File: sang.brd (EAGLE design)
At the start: 92.4 x 80 mm, 27 parts, among them IC1 L293D, IC2 L293D, IC3 NE555, Q1 16MHz

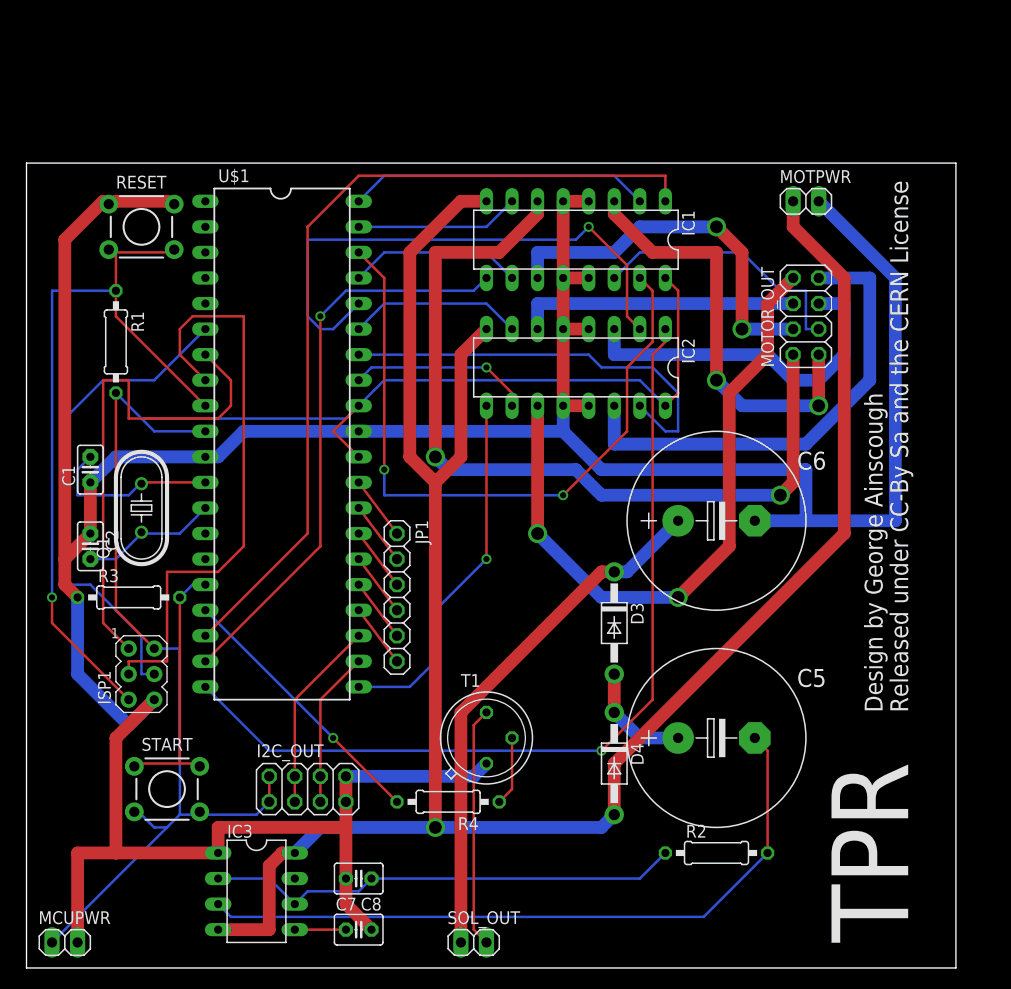
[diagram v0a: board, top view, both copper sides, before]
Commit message: Pins BrokenOut - Pullups Changed
Internal Pull ups to be used, aded I2C pullups
Broke ut unused pin
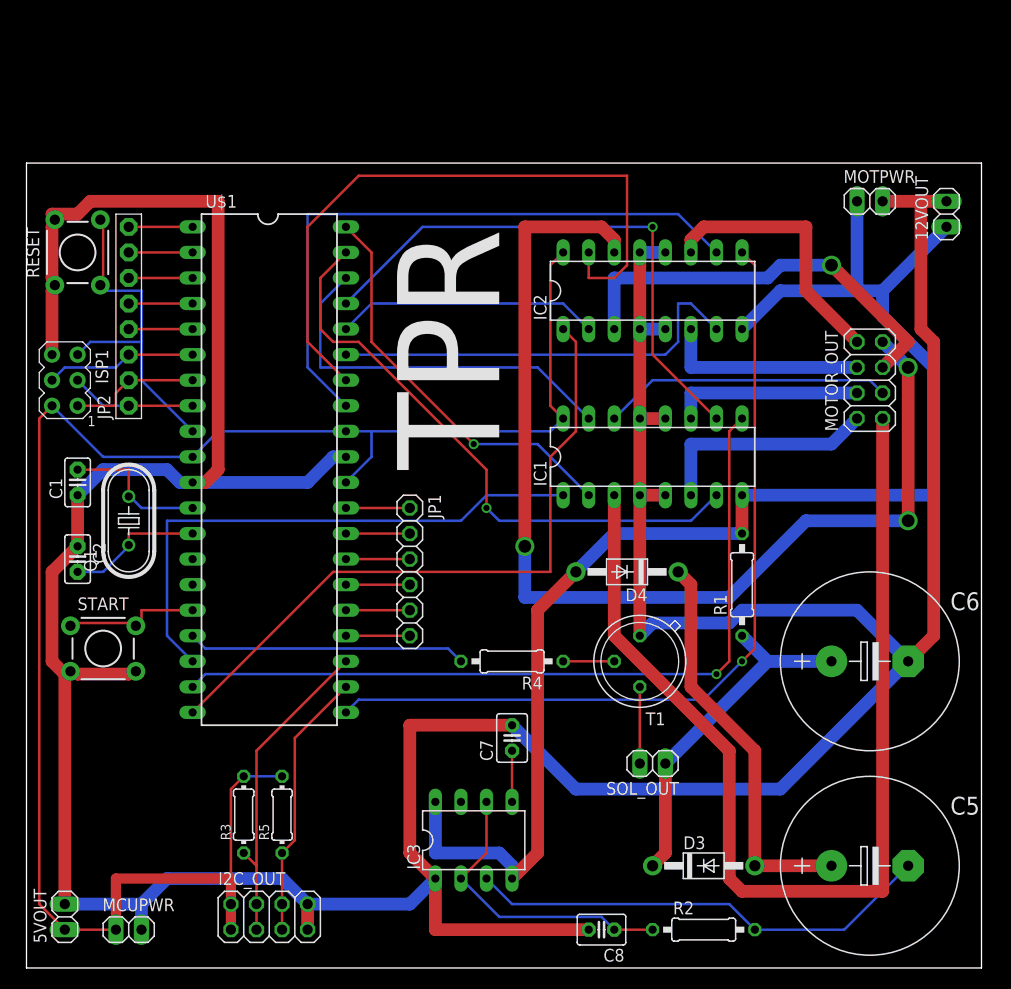
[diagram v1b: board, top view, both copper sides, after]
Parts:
- added 12VOUT, 5VOUT: (no value), pinhead:1X02
- added JP2: (no value), adafruit:1X08-BIG
- added R5: (no value), resistor:0204/7
- R3: value 10K -> (none); device resistor:0207/10 -> resistor:0204/7
- moved R1 66.7 mm to (71.1, 38.1), turned to 90 degrees
- moved ISP1 30.2 mm to (3.81, 58.4), turned to 180 degrees
- moved D3 25.7 mm to (67.3, 10.2), turned to 0 degrees
- moved SOL_OUT 25.1 mm to (62.2, 20.3), turned to 180 degrees
- moved C8 24.7 mm to (57.1, 3.81)
- moved R3 24.4 mm to (21.6, 15.2), turned to 90 degrees
- moved C7 24.4 mm to (48.3, 22.9), turned to 90 degrees
- moved IC1 22.9 mm to (62.2, 50.8), turned to 0 degrees
- moved IC3 22.2 mm to (44.5, 12.7), turned to 0 degrees
- moved C6 20.7 mm to (83.8, 30.5)
- moved C5 19.8 mm to (83.8, 10.2)
- moved D4 19.1 mm to (59.7, 39.4), turned to 180 degrees
- moved T1 17.0 mm to (61.0, 30.5), turned to 180 degrees
- moved R4 15.3 mm to (48.3, 30.5)
- moved START 15.3 mm to (7.62, 31.8)
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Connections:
- new net N$15: JP2.8, U$1.1
- new net N$16: JP2.7, U$1.2
- new net N$17: JP2.6, U$1.3
- new net N$18: JP2.5, U$1.4
- new net N$19: JP2.4, U$1.5
- net +12V: now also 12VOUT.1, R1.2
- net +24V: now also R1.1
- net +5V: now also 5VOUT.1, R3.2, R5.2; no longer R1.2, START.3, START.4
- net GND: now also 12VOUT.2, 5VOUT.2, START.3, START.4; no longer R3.1
- net GO: no longer R3.2
- net MISO: now also JP2.2
- net MOSI: now also JP2.3
- net RST: no longer R1.1
- net SCK: now also JP2.1
- net SCL: now also R5.1
- net SDA: now also R3.1
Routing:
- net GND: track 323.3 -> 410.6 mm
- net M1+: track 42.0 -> 105.6 mm, vias 2 -> 0
- net +12V: track 205.6 -> 144.4 mm, vias 1 -> 0
- net M1-: track 83.7 -> 22.6 mm, vias 2 -> 0
- net M4+: track 47.1 -> 107.6 mm, vias 0 -> 3
- net M4PWM: track 36.2 -> 83.2 mm
- net SCK: track 58.5 -> 12.5 mm
- net M4R: track 18.1 -> 62.8 mm, vias 1 -> 0
- net M1R: track 16.3 -> 59.2 mm, vias 0 -> 1
- net RST: track 75.7 -> 34.0 mm, vias 1 -> 0
- net M4-: track 65.8 -> 26.8 mm, vias 2 -> 0
- net M2R: track 17.3 -> 55.3 mm, vias 0 -> 1
- net MISO: track 50.9 -> 13.2 mm
- net MOSI: track 49.0 -> 15.0 mm
- net M2F: track 68.8 -> 38.7 mm, vias 2 -> 0
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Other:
- board size 92.4 x 80 mm -> 94.9 x 80 mm
- board text removed: "Design by George Ainscough"
- board text removed: "Released under CC-By Sa and the CERN License"
